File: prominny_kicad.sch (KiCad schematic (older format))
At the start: 17 parts

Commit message: finished the schematics, so far
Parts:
- added Brd?: SSD1306, symbol SSD1306-128x64_OLED:SSD1306
- added JP? (x7): Jumper_NO_Small, symbol Device:Jumper_NO_Small
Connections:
- net GND: now also JP?.1, JP?.1
- net VCC: now also JP?.1, JP?.1
- net scl: now also JP?.1, JP?.1
- net sda: now also JP?.1, JP?.1
- net at JP?.2: now also Brd?.3 (SCL), JP?.2
- new net: Brd?.1 (GND), JP?.2, JP?.2
- new net: Brd?.2 (VCC), JP?.2, JP?.2
- new net: Brd?.4 (SDA), JP?.2, JP?.2
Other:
- moved on the sheet: JP?, R?
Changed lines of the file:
@@
 Wire Wire Line
 	6500 2400 7000 2400
-Text GLabel 3500 3500 0    50   Input ~ 0
+Text GLabel 6100 6650 0    50   Input ~ 0
 sda
-Text GLabel 3500 4000 0    50   Input ~ 0
+Text GLabel 6100 7150 0    50   Input ~ 0
 scl
 Text GLabel 3300 2100 2    50   Input ~ 0
@@
 L power:VCC #PWR?
 U 1 1 5F93DF4B
-P 4000 3500
-F 0 "#PWR?" H 4000 3350 50  0001 C CNN
-F 1 "VCC" H 4015 3673 50  0000 C CNN
-F 2 "" H 4000 3500 50  0001 C CNN
-F 3 "" H 4000 3500 50  0001 C CNN
-	1    4000 3500
+P 6600 6650
+F 0 "#PWR?" H 6600 6500 50  0001 C CNN
+F 1 "VCC" H 6615 6823 50  0000 C CNN
+F 2 "" H 6600 6650 50  0001 C CNN
+F 3 "" H 6600 6650 50  0001 C CNN
+	1    6600 6650
 	1    0    0    -1
 $EndComp
@@
 L power:VCC #PWR?
 U 1 1 5F93E60B
-P 4000 4000
-F 0 "#PWR?" H 4000 3850 50  0001 C CNN
-F 1 "VCC" H 4015 4173 50  0000 C CNN
-F 2 "" H 4000 4000 50  0001 C CNN
-F 3 "" H 4000 4000 50  0001 C CNN
-	1    4000 4000
-	1    0    0    -1
-$EndComp
-Wire Wire Line
-	3500 3500 3600 3500
-Wire Wire Line
-	3500 4000 3600 4000
+P 6600 7150
+F 0 "#PWR?" H 6600 7000 50  0001 C CNN
+F 1 "VCC" H 6615 7323 50  0000 C CNN
+F 2 "" H 6600 7150 50  0001 C CNN
+F 3 "" H 6600 7150 50  0001 C CNN
+	1    6600 7150
+	1    0    0    -1
+$EndComp
+Wire Wire Line
+	6100 6650 6200 6650
+Wire Wire Line
+	6100 7150 6200 7150
 $Comp
 L Device:R_Small R?
 U 1 1 5F944BD1
-P 3700 4000
-F 0 "R?" V 3504 4000 50  0000 C CNN
-F 1 "4.7k" V 3595 4000 50  0000 C CNN
-F 2 "" H 3700 4000 50  0001 C CNN
-F 3 "~" H 3700 4000 50  0001 C CNN
-	1    3700 4000
+P 6300 7150
+F 0 "R?" V 6104 7150 50  0000 C CNN
+F 1 "4.7k" V 6195 7150 50  0000 C CNN
+F 2 "" H 6300 7150 50  0001 C CNN
+F 3 "~" H 6300 7150 50  0001 C CNN
+	1    6300 7150
 	0    1    1    0
 $EndComp
@@
 L Device:R_Small R?
 U 1 1 5F945A1E
-P 3700 3500
-F 0 "R?" V 3504 3500 50  0000 C CNN
-F 1 "4.7k" V 3595 3500 50  0000 C CNN
-F 2 "" H 3700 3500 50  0001 C CNN
-F 3 "~" H 3700 3500 50  0001 C CNN
-	1    3700 3500
+P 6300 6650
+F 0 "R?" V 6104 6650 50  0000 C CNN
+F 1 "4.7k" V 6195 6650 50  0000 C CNN
+F 2 "" H 6300 6650 50  0001 C CNN
+F 3 "~" H 6300 6650 50  0001 C CNN
+	1    6300 6650
 	0    1    1    0
 $EndComp
 Wire Wire Line
-	3800 3500 4000 3500
-Wire Wire Line
-	3800 4000 4000 4000
+	6400 6650 6600 6650
+Wire Wire Line
+	6400 7150 6600 7150
 $Comp
 L Device:Jumper_NO_Small JP?
 U 1 1 5F94E6CB
-P 4650 4100
-F 0 "JP?" H 4650 4285 50  0000 C CNN
-F 1 "Jumper_NO_Small" H 4650 4194 50  0000 C CNN
-F 2 "" H 4650 4100 50  0001 C CNN
-F 3 "~" H 4650 4100 50  0001 C CNN
-	1    4650 4100
-	1    0    0    -1
-$EndComp
+P 6500 5100
+F 0 "JP?" H 6500 5285 50  0000 C CNN
+F 1 "Jumper_NO_Small" H 6500 5194 50  0000 C CNN
+F 2 "" H 6500 5100 50  0001 C CNN
+F 3 "~" H 6500 5100 50  0001 C CNN
+	1    6500 5100
+	1    0    0    -1
+$EndComp
+$Comp
+L SSD1306-128x64_OLED:SSD1306 Brd?
+U 1 1 5F954526
+P 7250 5150
+F 0 "Brd?" V 7296 4872 50  0000 R CNN
+F 1 "SSD1306" V 7205 4872 50  0000 R CNN
+F 2 "" H 7250 5400 50  0001 C CNN
+F 3 "" H 7250 5400 50  0001 C CNN
+	1    7250 5150
+	0    -1   -1   0
+$EndComp
+Text GLabel 6000 5000 0    50   Input ~ 0
+sda
+Text GLabel 6000 5100 0    50   Input ~ 0
+scl
+$Comp
+L Device:Jumper_NO_Small JP?
+U 1 1 5F967B39
+P 6500 5000
+F 0 "JP?" H 6500 5185 50  0000 C CNN
+F 1 "Jumper_NO_Small" H 6500 5094 50  0000 C CNN
+F 2 "" H 6500 5000 50  0001 C CNN
+F 3 "~" H 6500 5000 50  0001 C CNN
+	1    6500 5000
+	1    0    0    -1
+$EndComp
+Text GLabel 6000 5300 0    50   Input ~ 0
+ground
+Text GLabel 6000 5200 0    50   Input ~ 0
+power
+$Comp
+L Device:Jumper_NO_Small JP?
+U 1 1 5F985423
+P 6500 5200
+F 0 "JP?" H 6500 5385 50  0000 C CNN
+F 1 "Jumper_NO_Small" H 6500 5294 50  0000 C CNN
+F 2 "" H 6500 5200 50  0001 C CNN
+F 3 "~" H 6500 5200 50  0001 C CNN
+	1    6500 5200
+	1    0    0    -1
+$EndComp
+$Comp
+L Device:Jumper_NO_Small JP?
+U 1 1 5F985958
+P 6500 5300
+F 0 "JP?" H 6500 5485 50  0000 C CNN
+F 1 "Jumper_NO_Small" H 6500 5394 50  0000 C CNN
+F 2 "" H 6500 5300 50  0001 C CNN
+F 3 "~" H 6500 5300 50  0001 C CNN
+	1    6500 5300
+	1    0    0    -1
+$EndComp
+$Comp
+L Device:Jumper_NO_Small JP?
+U 1 1 5F98B0FF
+P 6500 5600
+F 0 "JP?" H 6500 5785 50  0000 C CNN
+F 1 "Jumper_NO_Small" H 6500 5694 50  0000 C CNN
+F 2 "" H 6500 5600 50  0001 C CNN
+F 3 "~" H 6500 5600 50  0001 C CNN
+	1    6500 5600
+	1    0    0    -1
+$EndComp
+$Comp
+L Device:Jumper_NO_Small JP?
+U 1 1 5F98B105
+P 6500 5500
+F 0 "JP?" H 6500 5685 50  0000 C CNN
+F 1 "Jumper_NO_Small" H 6500 5594 50  0000 C CNN
+F 2 "" H 6500 5500 50  0001 C CNN
+F 3 "~" H 6500 5500 50  0001 C CNN
+	1    6500 5500
+	1    0    0    -1
+$EndComp
+$Comp
+L Device:Jumper_NO_Small JP?
+U 1 1 5F98B10B
+P 6500 5700
+F 0 "JP?" H 6500 5885 50  0000 C CNN
+F 1 "Jumper_NO_Small" H 6500 5794 50  0000 C CNN
+F 2 "" H 6500 5700 50  0001 C CNN
+F 3 "~" H 6500 5700 50  0001 C CNN
+	1    6500 5700
+	1    0    0    -1
+$EndComp
+$Comp
+L Device:Jumper_NO_Small JP?
+U 1 1 5F98B111
+P 6500 5800
+F 0 "JP?" H 6500 5985 50  0000 C CNN
+F 1 "Jumper_NO_Small" H 6500 5894 50  0000 C CNN
+F 2 "" H 6500 5800 50  0001 C CNN
+F 3 "~" H 6500 5800 50  0001 C CNN
+	1    6500 5800
+	1    0    0    -1
+$EndComp
+Wire Wire Line
+	6000 5000 6400 5000
+Wire Wire Line
+	6000 5100 6400 5100
+Wire Wire Line
+	6000 5200 6400 5200
+Wire Wire Line
+	6000 5300 6400 5300
+Wire Wire Line
+	6600 5000 6650 5000
+Wire Wire Line
+	6600 5100 6700 5100
+Wire Wire Line
+	6600 5200 6750 5200
+Wire Wire Line
+	6600 5300 6800 5300
+Wire Wire Line
+	6600 5500 6650 5500
+Wire Wire Line
+	6650 5500 6650 5000
+Connection ~ 6650 5000
+Wire Wire Line
+	6650 5000 6900 5000
+Wire Wire Line
+	6600 5600 6700 5600
+Wire Wire Line
+	6700 5600 6700 5100
+Connection ~ 6700 5100
+Wire Wire Line
+	6700 5100 6900 5100
+Wire Wire Line
+	6600 5700 6750 5700
+Wire Wire Line
+	6750 5700 6750 5200
+Connection ~ 6750 5200
+Wire Wire Line
+	6750 5200 6900 5200
+Wire Wire Line
+	6600 5800 6800 5800
+Wire Wire Line
+	6800 5800 6800 5300
+Connection ~ 6800 5300
+Wire Wire Line
+	6800 5300 6900 5300
+Text GLabel 6000 5500 0    50   Input ~ 0
+ground
+Text GLabel 6000 5600 0    50   Input ~ 0
+power
+Text GLabel 6000 5700 0    50   Input ~ 0
+scl
+Text GLabel 6000 5800 0    50   Input ~ 0
+sda
+Wire Wire Line
+	6000 5500 6400 5500
+Wire Wire Line
+	6000 5600 6400 5600
+Wire Wire Line
+	6000 5700 6400 5700
+Wire Wire Line
+	6000 5800 6400 5800
 $EndSCHEMATC

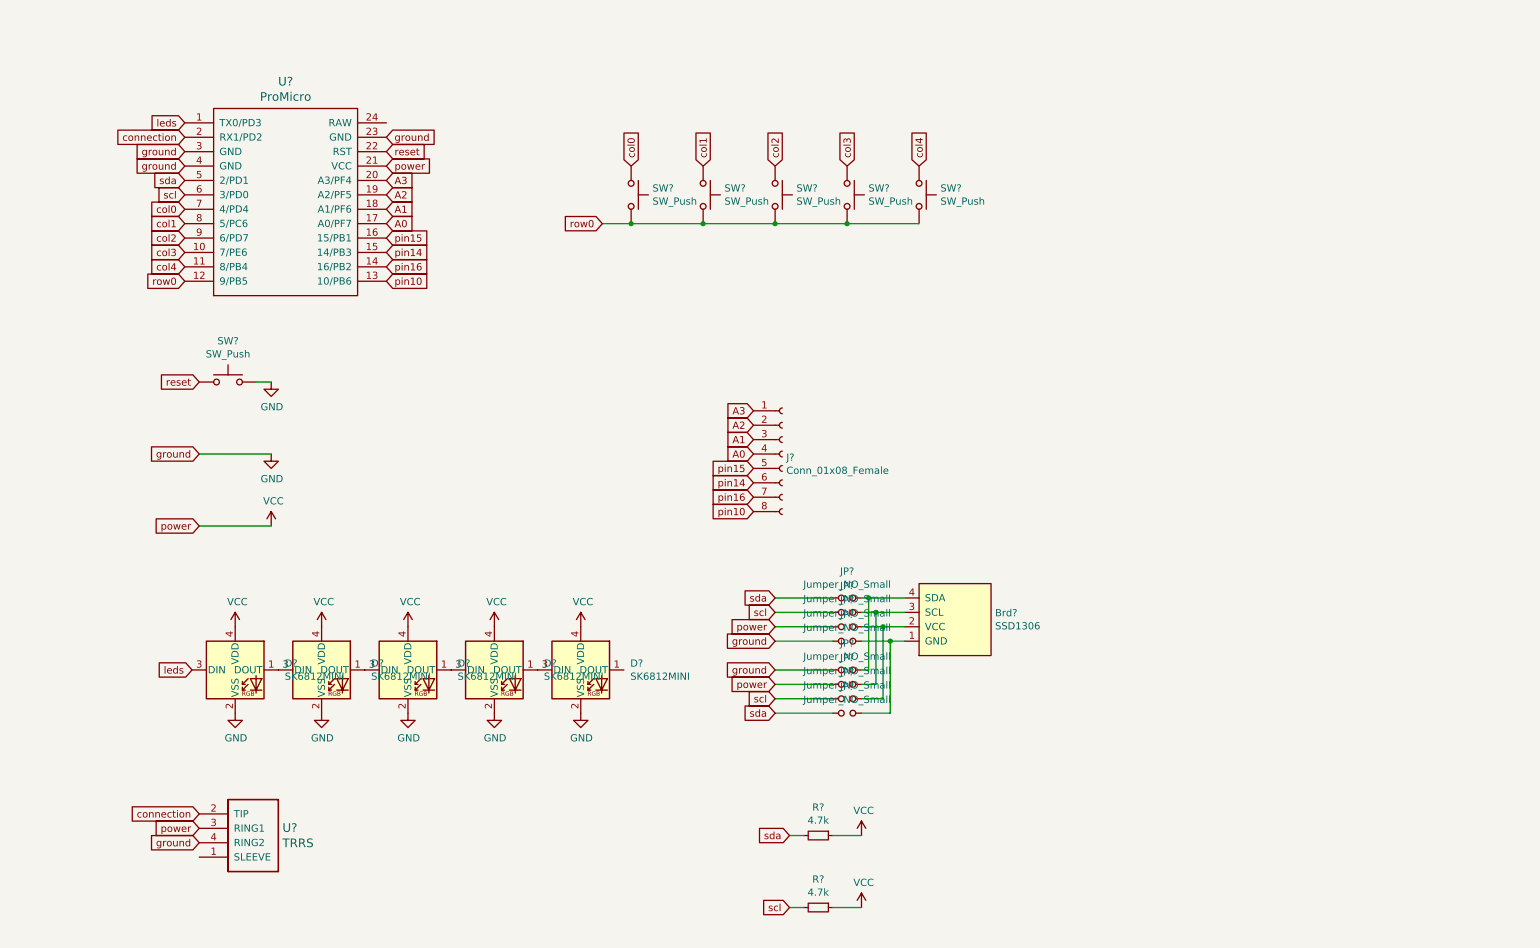
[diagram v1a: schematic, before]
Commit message: - started the PCB design - finished the schematics (a second time ) - changed the LEDs to ws2812b (per key doesn't make sense with 5 keys)
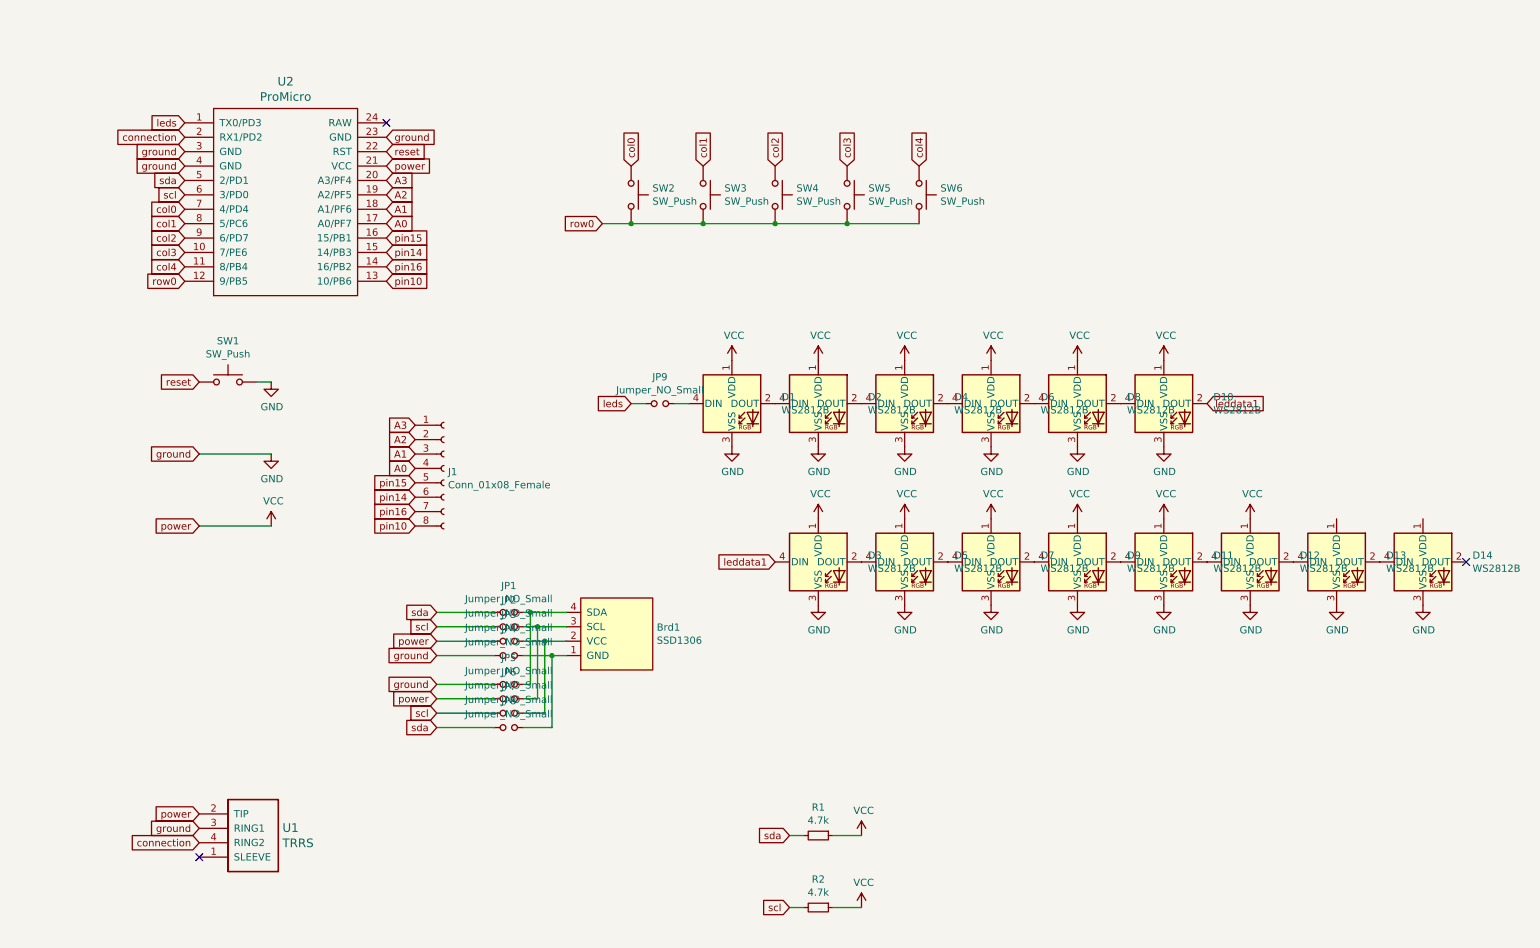
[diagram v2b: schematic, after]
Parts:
- removed D? (x5): SK6812MINI, LED_SMD:LED_SK6812MINI_PLCC4_3.5x3.5mm_P1.75mm, symbol LED:SK6812MINI
- added D1, D10, D11, D12, D13, D14, D2, D3, D4, D5, D6, D7, D8, D9: WS2812B, LED_SMD:LED_WS2812B_PLCC4_5.0x5.0mm_P3.2mm, symbol LED:WS2812B
- added JP9: Jumper_NO_Small, Jumper:SolderJumper-2_P1.3mm_Open_Pad1.0x1.5mm, symbol Device:Jumper_NO_Small
- Brd1: renamed from Brd?; footprint (none) -> SSD1306:128x64OLED
- J1: renamed from J?; footprint (none) -> Connector_PinHeader_1.00mm:PinHeader_1x08_P1.00mm_Vertical
- JP1, JP2, JP3, JP4, JP5, JP6, JP7, JP8: renamed from JP?; footprint (none) -> Jumper:SolderJumper-2_P1.3mm_Open_Pad1.0x1.5mm
- R1, R2: renamed from R?; footprint (none) -> Resistor_SMD:R_0805_2012Metric
- SW1: renamed from SW?; footprint (none) -> Keebio-Parts:SW_SPST_TL3342
- SW2: renamed from SW?; footprint (none) -> Keebio-Parts:Low-Profile-Choc-MX
- SW3, SW4, SW5, SW6: renamed from SW?; footprint (none) -> Keebio-Parts:Cherry-MX-Low-Profile
- U1: renamed from U?; footprint (none) -> Keebio-Parts:TRRS-PJ-320A-dual
- U2: renamed from U?; footprint (none) -> Keebio-Parts:ArduinoProMicro
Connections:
- net GND: now also U1.3 (RING1), D1.3 (VSS), D10.3 (VSS), D11.3 (VSS), D12.3 (VSS), D13.3 (VSS), D14.3 (VSS), D2.3 (VSS), D3.3 (VSS), D4.3 (VSS), D5.3 (VSS), D6.3 (VSS), D7.3 (VSS), D8.3 (VSS), D9.3 (VSS); no longer U1.4 (RING2)
- net VCC: now also U1.2 (TIP), D1.1 (VDD), D10.1 (VDD), D11.1 (VDD), D12.1 (VDD), D2.1 (VDD), D3.1 (VDD), D4.1 (VDD), D5.1 (VDD), D6.1 (VDD), D7.1 (VDD), D8.1 (VDD), D9.1 (VDD); no longer U1.3 (RING1)
- net connection: now also U1.4 (RING2); no longer U1.2 (TIP)
- net leds: now also JP9.1
- new net: D10.4 (DIN), D8.2 (DOUT)
- new net: D6.2 (DOUT), D8.4 (DIN)
- new net: D3.2 (DOUT), D5.4 (DIN)
- new net: D5.2 (DOUT), D7.4 (DIN)
- new net: D7.2 (DOUT), D9.4 (DIN)
- new net: D11.4 (DIN), D9.2 (DOUT)
- new net: D11.2 (DOUT), D12.4 (DIN)
- new net: D12.2 (DOUT), D13.4 (DIN)
- new net: D13.2 (DOUT), D14.4 (DIN)
- new net: D1.4 (DIN), JP9.2
- new net: D1.2 (DOUT), D2.4 (DIN)
- new net: D2.2 (DOUT), D4.4 (DIN)
- new net: D4.2 (DOUT), D6.4 (DIN)
- new net leddata1: D10.2 (DOUT), D3.4 (DIN)
- no-connect marks 0 -> 3
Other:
- moved on the sheet: Brd1, J1, JP1, JP2, JP3, JP4, JP5, JP6, JP7, JP8

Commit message: arranges, added edgecuts, started routing
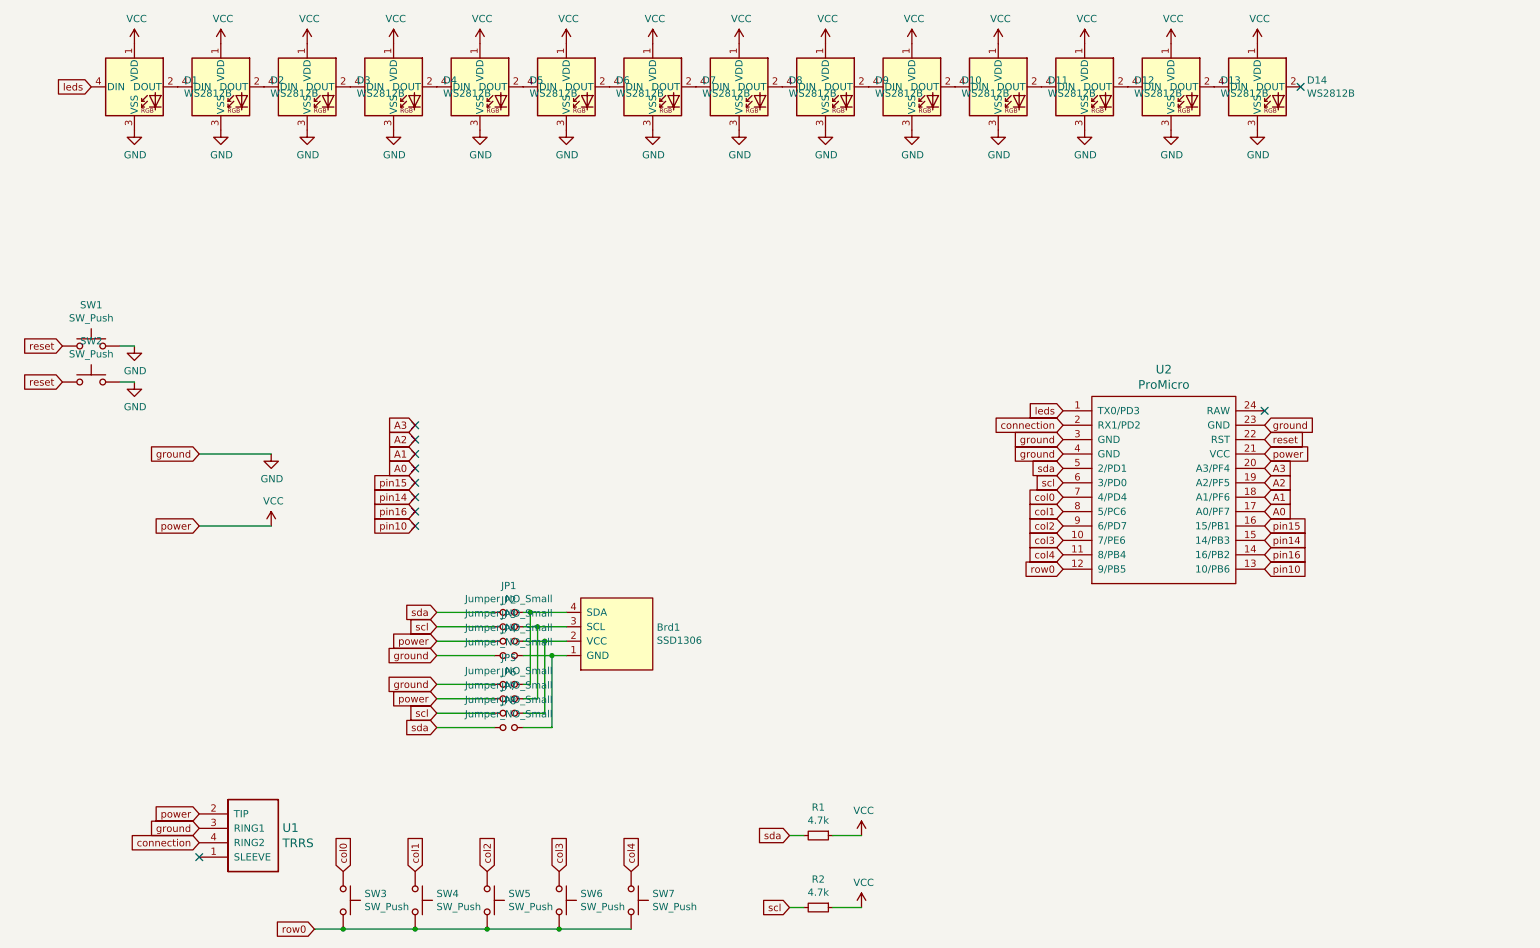
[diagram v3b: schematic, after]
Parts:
- removed J1: Conn_01x08_Female, Connector_PinHeader_1.00mm:PinHeader_1x08_P1.00mm_Vertical, symbol Connector:Conn_01x08_Female
- removed JP9: Jumper_NO_Small, Jumper:SolderJumper-2_P1.3mm_Open_Pad1.0x1.5mm, symbol Device:Jumper_NO_Small
- added SW2: SW_Push, Keebio-Parts:SW_SPST_TL3342, symbol Switch:SW_Push
- D1, D10, D11, D12, D13, D14, D2, D3, D4, D5, D6, D7, D8, D9: footprint LED_SMD:LED_WS2812B_PLCC4_5.0x5.0mm_P3.2mm -> Keebio-Parts:WS2812B
- SW3: renamed from SW2; footprint Keebio-Parts:Low-Profile-Choc-MX -> other_parts:CherryMX_Choc_1u_reversible
- SW4: renamed from SW3; footprint Keebio-Parts:Cherry-MX-Low-Profile -> other_parts:CherryMX_Choc_1u_reversible
- SW5: renamed from SW4; footprint Keebio-Parts:Cherry-MX-Low-Profile -> other_parts:CherryMX_Choc_1u_reversible
- SW6: renamed from SW5; footprint Keebio-Parts:Cherry-MX-Low-Profile -> other_parts:CherryMX_Choc_1u_reversible
- SW7: renamed from SW6; footprint Keebio-Parts:Cherry-MX-Low-Profile -> other_parts:CherryMX_Choc_1u_reversible
- U2: footprint Keebio-Parts:ArduinoProMicro -> other_parts:ProMicro
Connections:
- net GND: now also SW2.2
- net VCC: now also D13.1 (VDD), D14.1 (VDD)
- net leds: now also D1.4 (DIN)
- net reset: now also SW2.1
- net at D8.2 (DOUT): now also D9.4 (DIN); no longer D10.4 (DIN)
- net at D6.2 (DOUT): now also D7.4 (DIN); no longer D8.4 (DIN)
- net at D3.2 (DOUT): now also D4.4 (DIN); no longer D5.4 (DIN)
- net at D5.2 (DOUT): now also D6.4 (DIN); no longer D7.4 (DIN)
- net at D7.2 (DOUT): now also D8.4 (DIN); no longer D9.4 (DIN)
- net at D9.2 (DOUT): now also D10.4 (DIN); no longer D11.4 (DIN)
- net at D2.2 (DOUT): now also D3.4 (DIN); no longer D4.4 (DIN)
- net at D4.2 (DOUT): now also D5.4 (DIN); no longer D6.4 (DIN)
- net leddata1: no longer names the net of D10.2 (DOUT)
- net leddata1: now also D11.4 (DIN); no longer D3.4 (DIN)
- no-connect marks 3 -> 11
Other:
- moved on the sheet: SW1, SW3, SW4, SW5, SW6, SW7, U2

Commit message: removed the LEDs cause they're useless ans instead added a breakout to add a strip if needed. Finished routing
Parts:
- removed D1, D10, D11, D12, D13, D14, D2, D3, D4, D5, D6, D7, D8, D9: WS2812B, Keebio-Parts:WS2812B, symbol LED:WS2812B
- added J1: Conn_01x03, Connector_PinSocket_2.00mm:PinSocket_1x03_P2.00mm_Vertical, symbol Connector_Generic:Conn_01x03
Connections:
- net GND: now also J1.3 (Pin_3)
- net VCC: now also J1.2 (Pin_2)
- net leds: now also J1.1 (Pin_1)
- no-connect marks 11 -> 10
